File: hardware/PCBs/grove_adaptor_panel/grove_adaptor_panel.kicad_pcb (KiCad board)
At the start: 2 copper layers, 72 x 46.8 mm, 57 parts, among them J1 Conn_01x04, J2 Conn_01x04

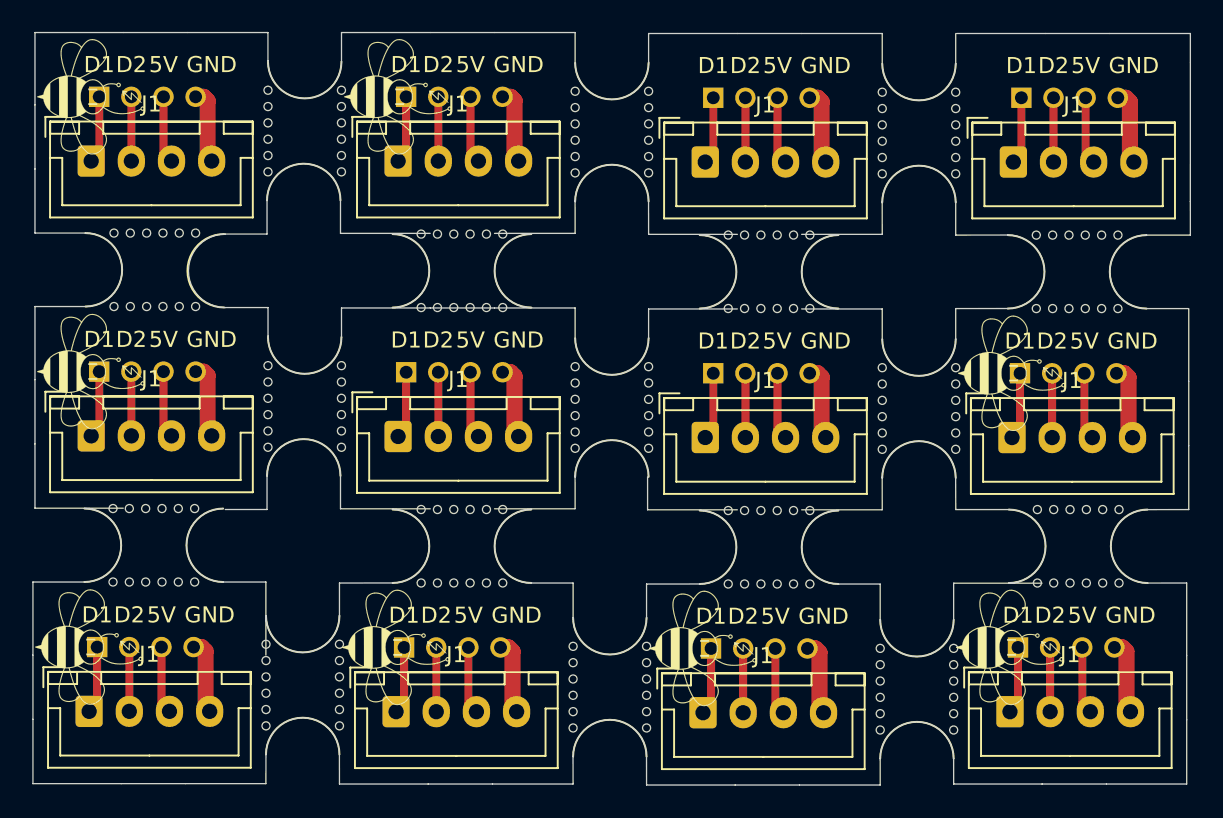
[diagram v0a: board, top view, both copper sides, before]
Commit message: Fix grove_adaptor_panel edge cuts (using KiCad 9)
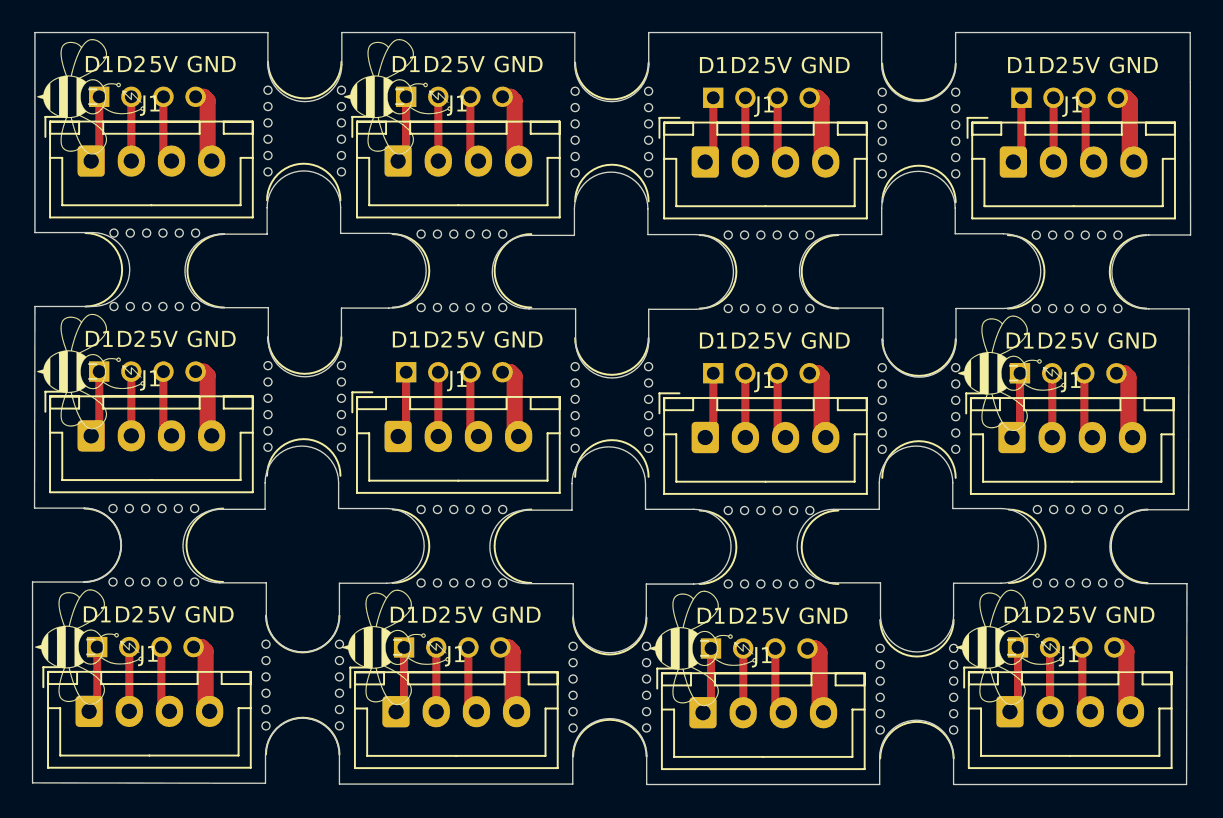
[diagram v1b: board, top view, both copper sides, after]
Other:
- board size 72 x 46.8 mm -> 72.1 x 46.8 mm
- net class Default removed
